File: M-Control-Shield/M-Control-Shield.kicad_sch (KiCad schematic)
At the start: 33 parts, among them J1 Conn_01x08, J2 Conn_01x06, J3 Conn_01x10, J4 Conn_01x08

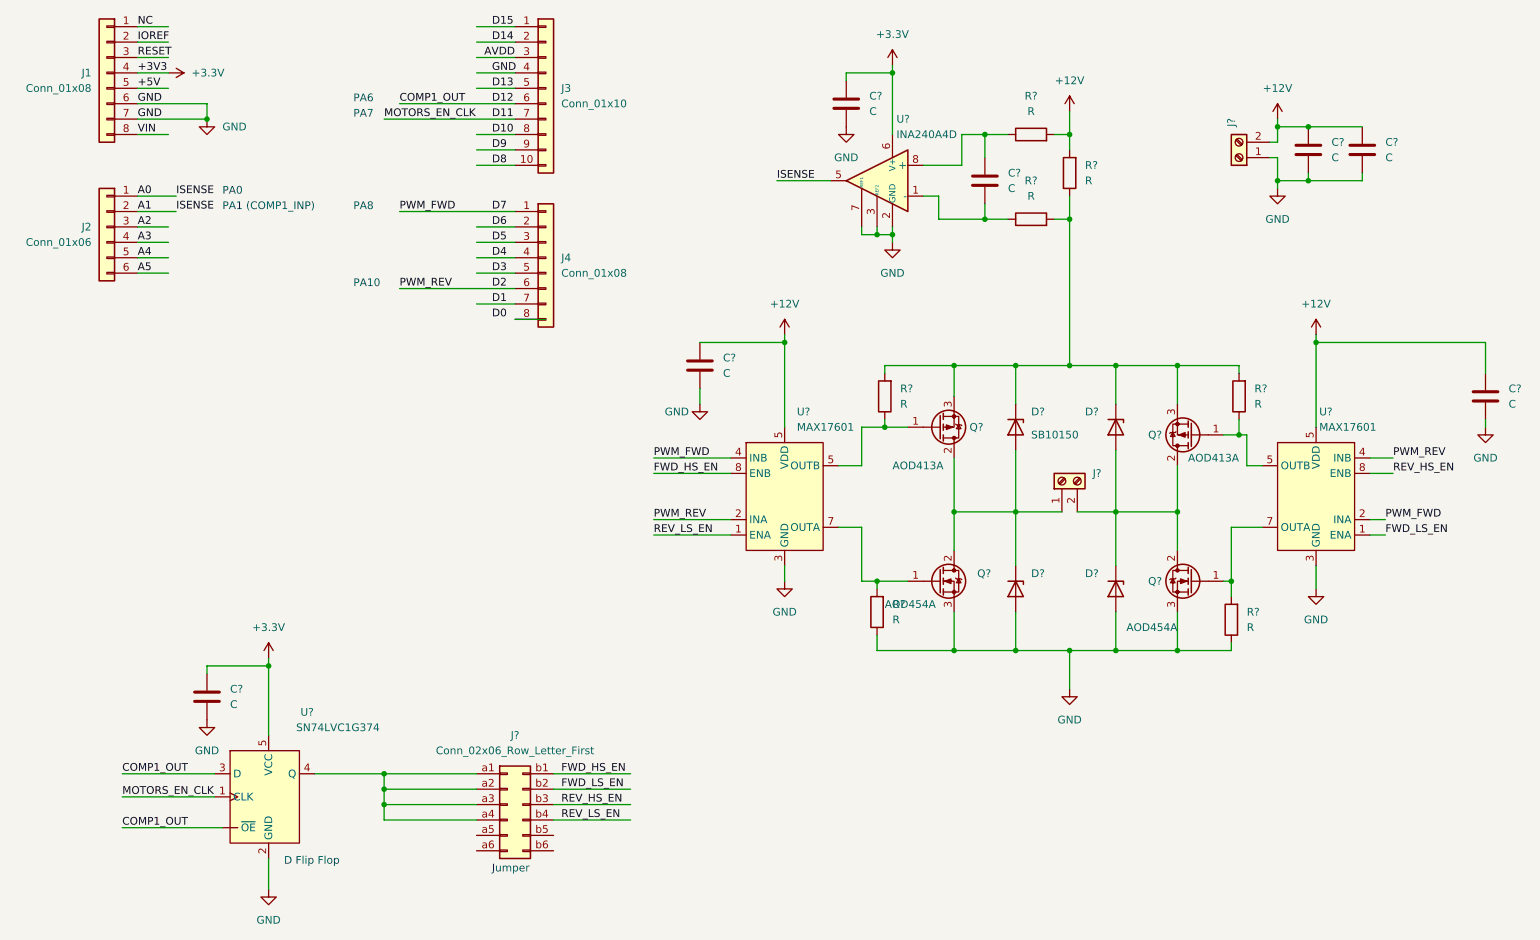
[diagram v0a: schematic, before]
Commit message: Annotated and imported to pcb
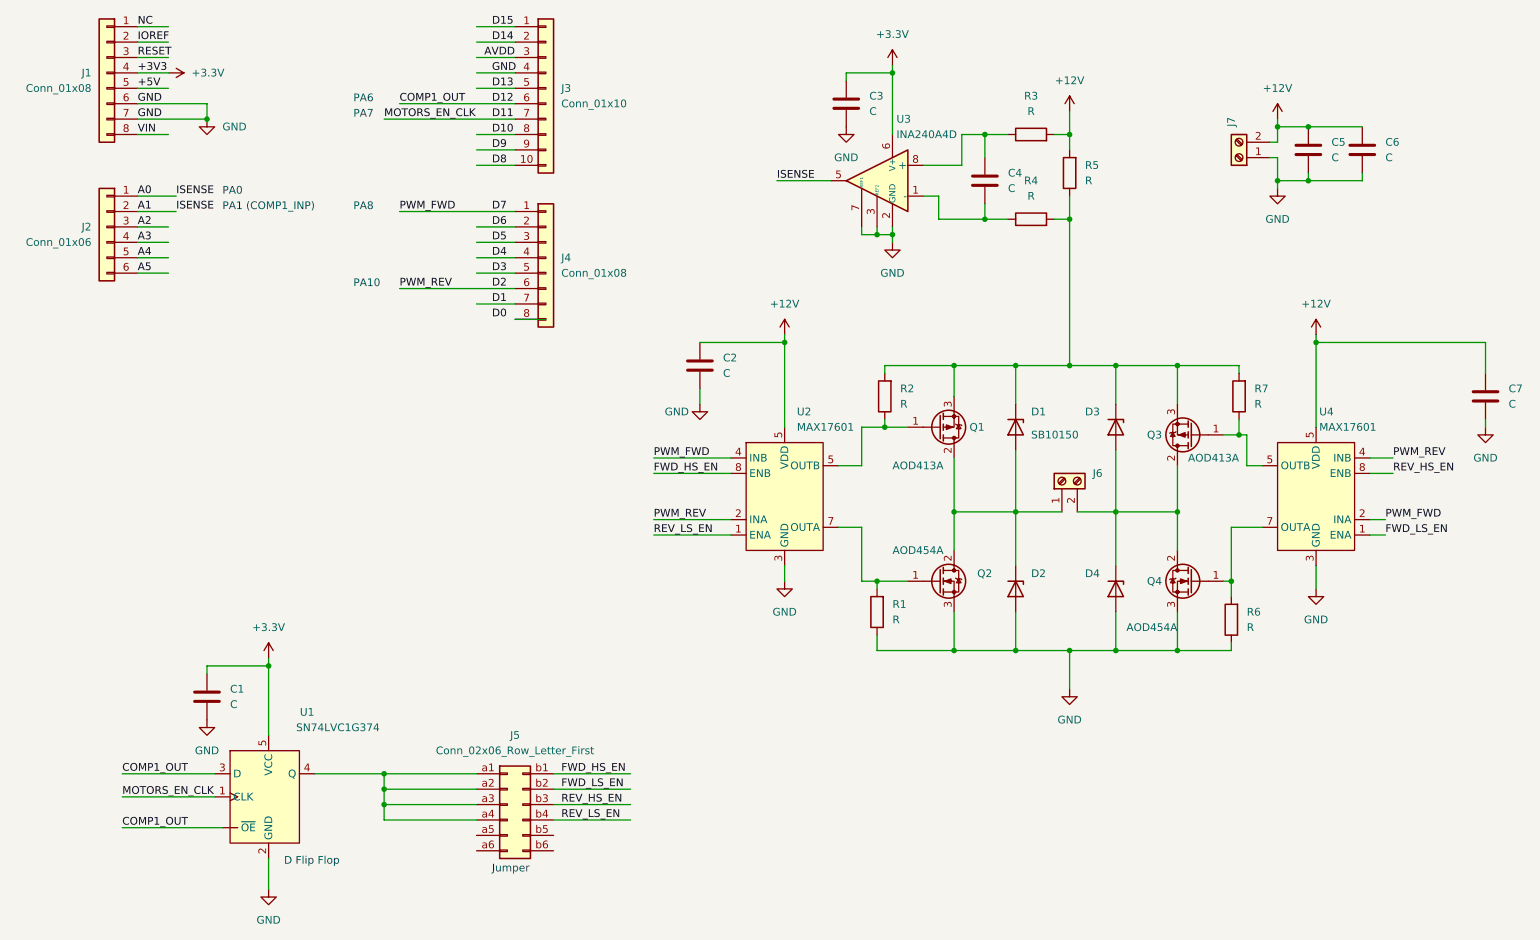
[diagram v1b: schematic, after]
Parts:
- gave numbers to parts that had none: 29
